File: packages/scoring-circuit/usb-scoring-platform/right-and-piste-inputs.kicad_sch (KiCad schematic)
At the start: 20 parts, among them J4 RIGHT WEAPON A B C, J5 PISTE - NOT protective earth, U9 74LVC125APW

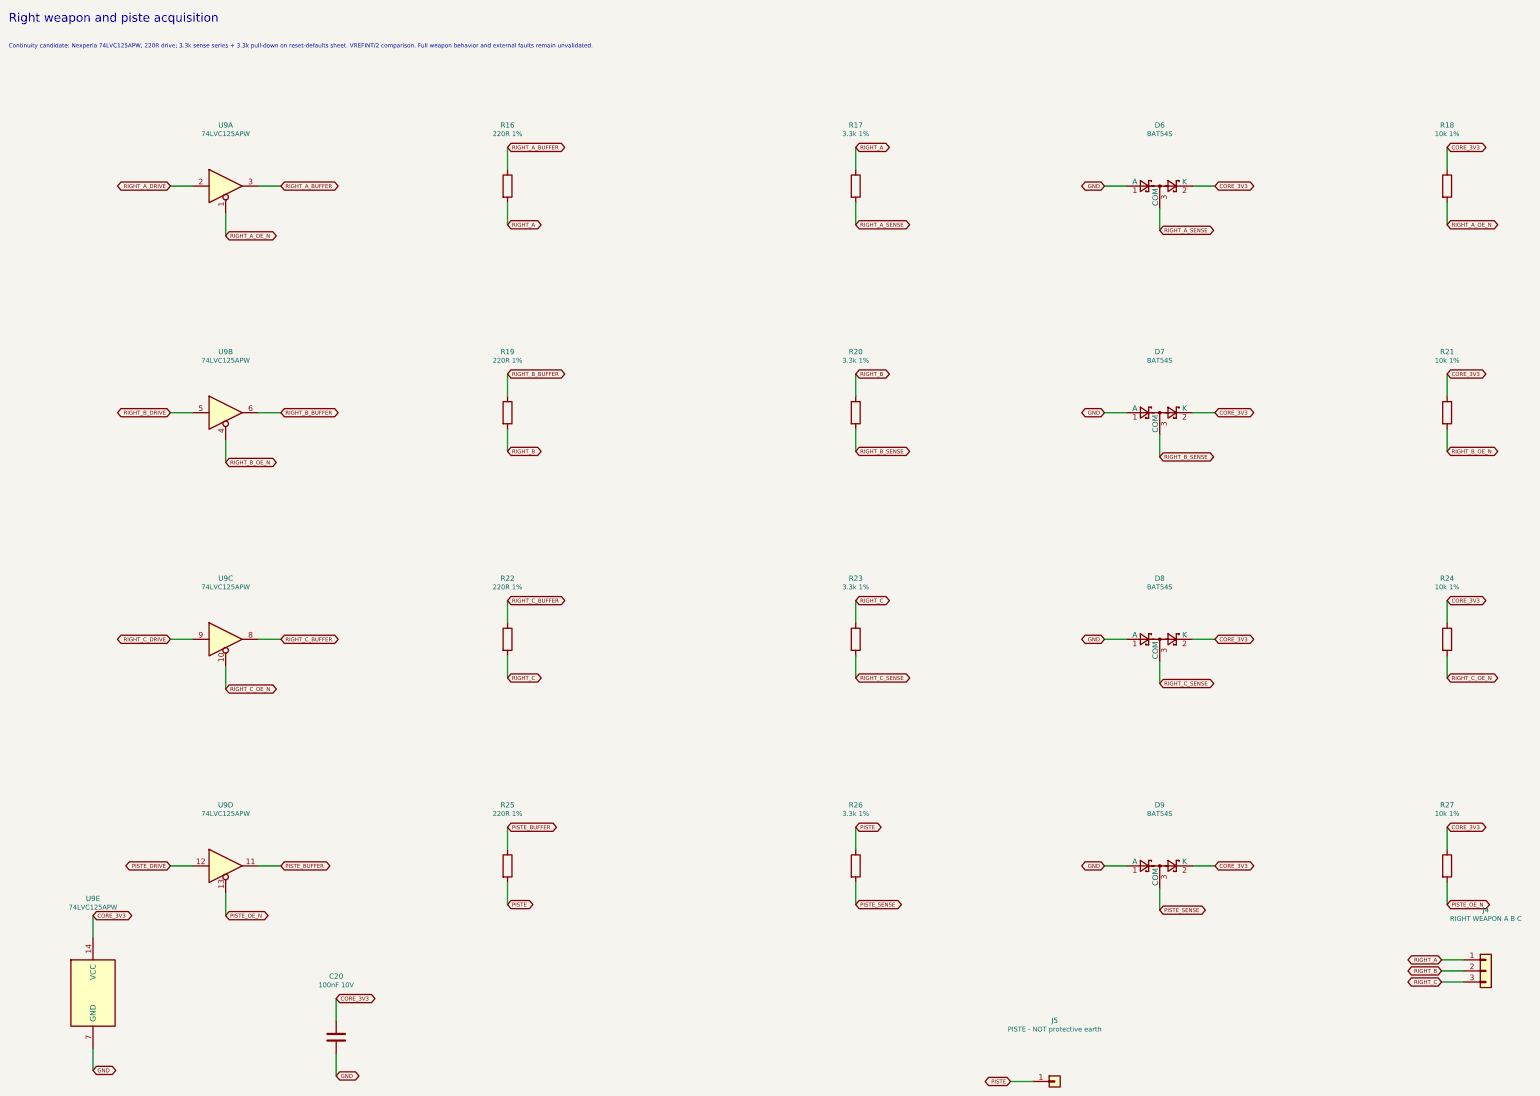
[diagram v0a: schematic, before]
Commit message: fix(scoring): shorten acquisition scan and qualify contact inputs
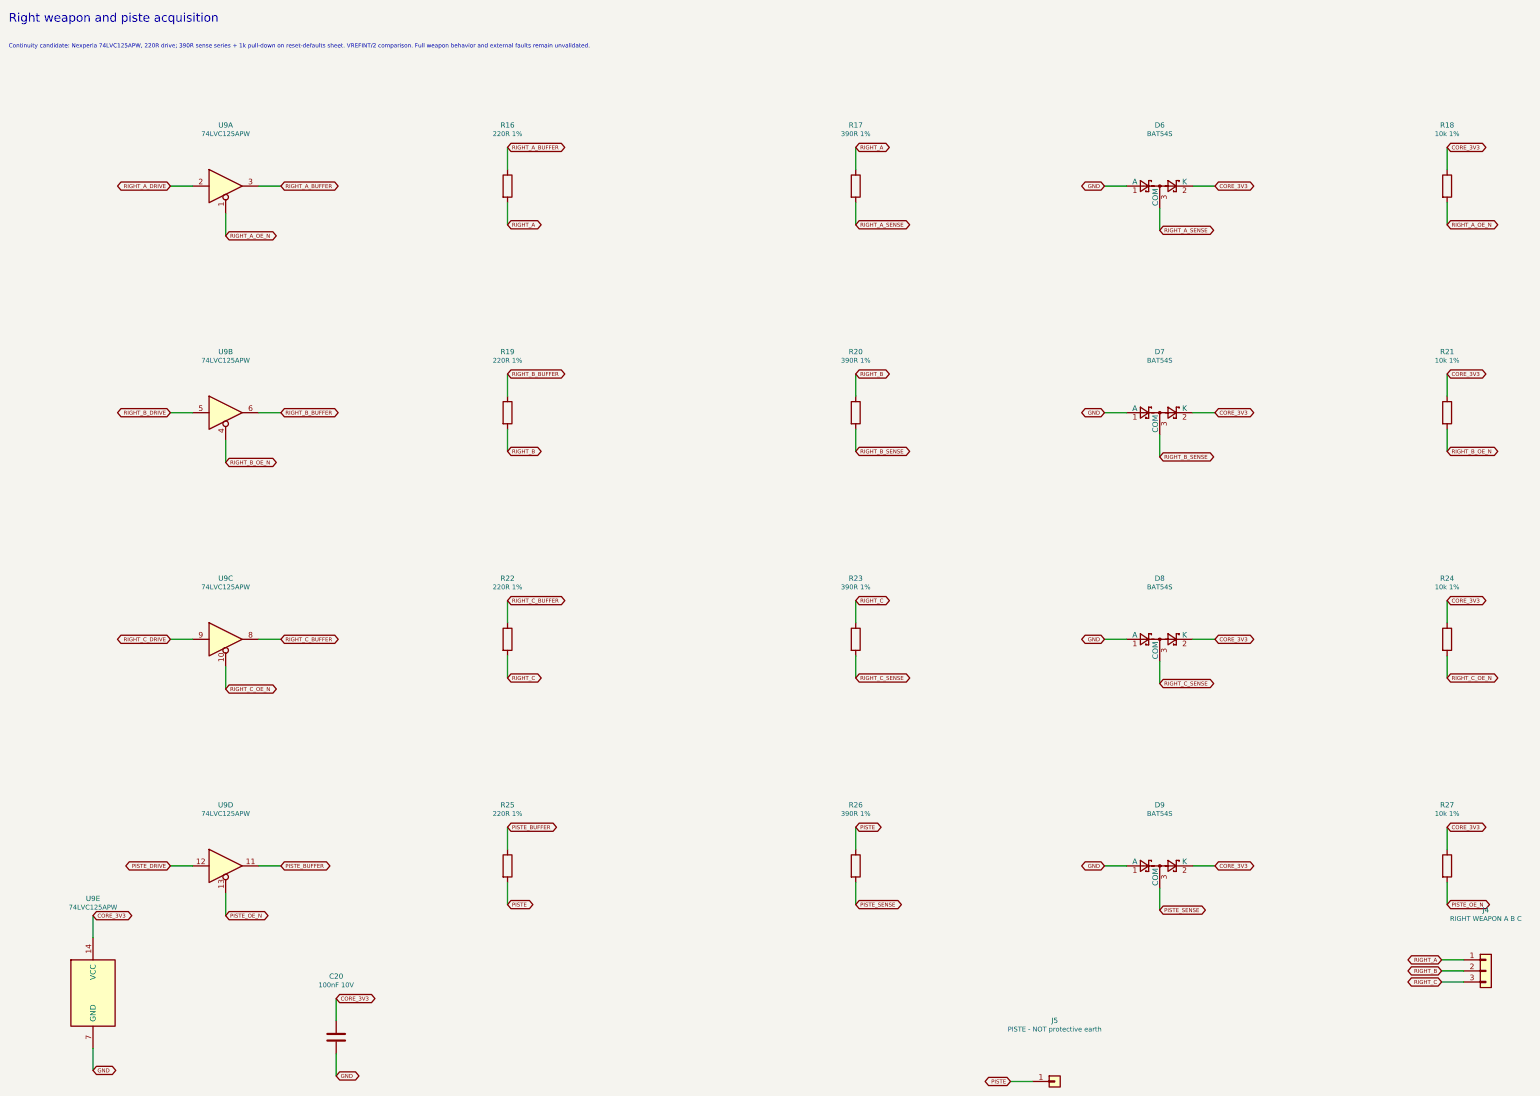
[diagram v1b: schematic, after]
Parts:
- R17, R20, R23, R26: value 3.3k 1% -> 390R 1%; MPN RC0603FR-073K3L -> RC0603FR-07390RL
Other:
- note added: "Continuity candidate: Nexperia 74LVC125APW, 220R drive; 390R sense series + 1k pull-down on reset-defaults sheet. VREFINT/2 comparison. Full weapon behavior and external faults remain unvalidated."
- note removed: "Continuity candidate: Nexperia 74LVC125APW, 220R drive; 3.3k sense series + 3.3k pull-down on reset-defaults sheet. VREFINT/2 comparison. Full weapon behavior and external faults remain unvalidated."

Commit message: fix(scoring-circuit): source stocked bypass and reservoir capacitors
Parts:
- C20: MPN C1608X7R1H104K080AA -> CC0603KRX7R9BB104; Manufacturer TDK -> Yageo
